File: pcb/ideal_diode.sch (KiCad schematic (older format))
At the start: 17 parts, among them P1 CONN_01X03, Q1 BSC028N06NS, Q2 BSC028N06NS, U1 LTC4359

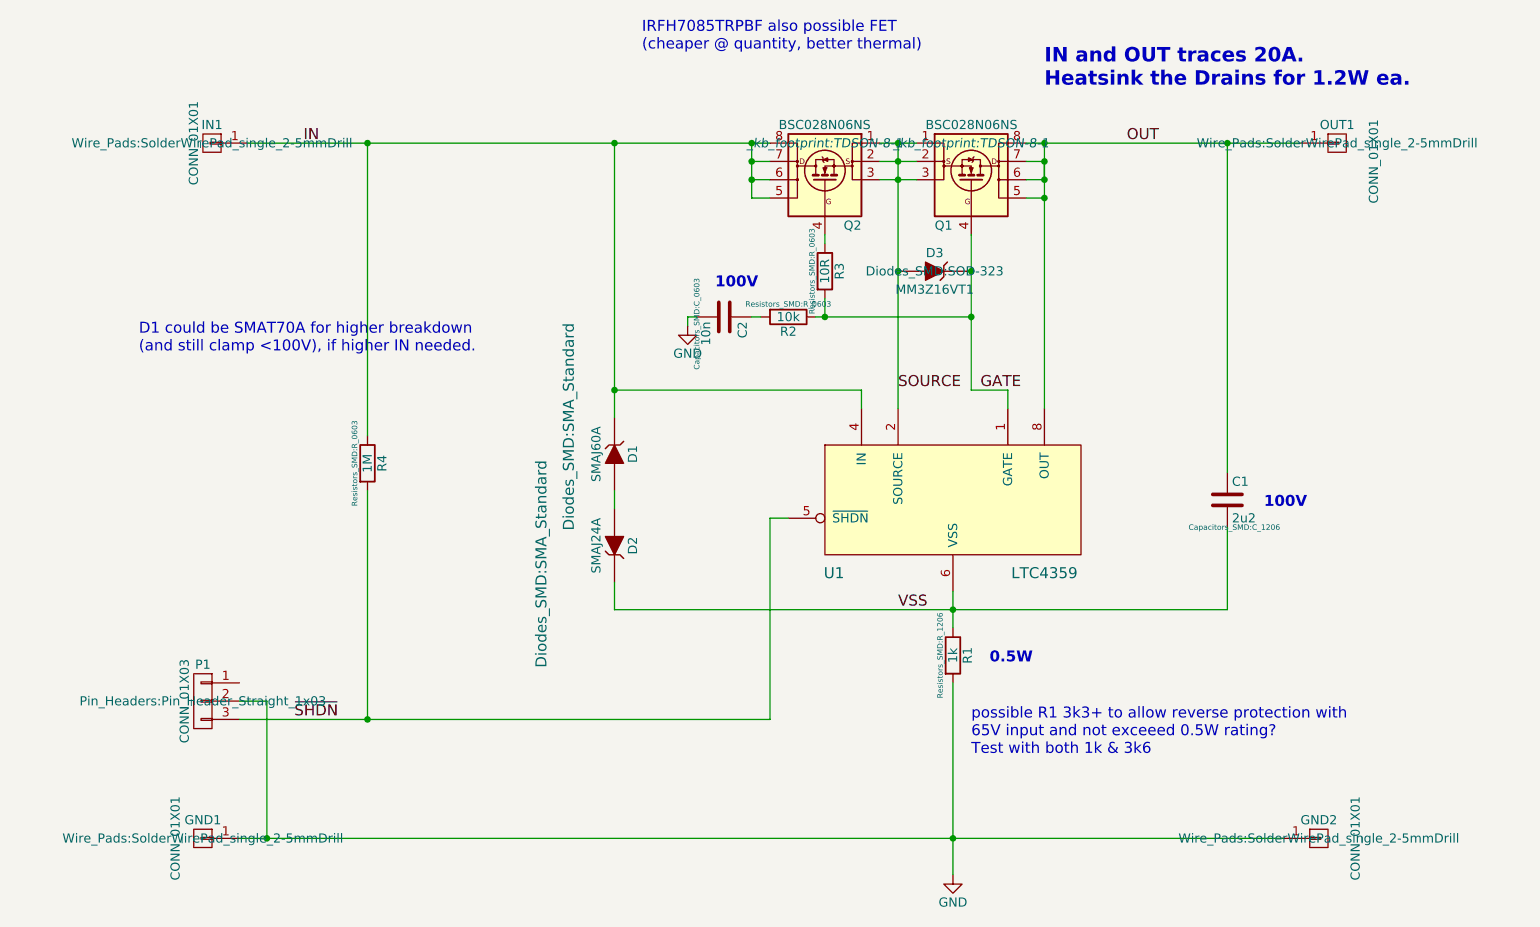
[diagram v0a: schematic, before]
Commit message: setting license as CERN OHL updating titleblocks ready for 1.0 release, added silkscreen ID & version. changed from 4V-70V to 5V-60V to reflect design capabilities changed R1 from 1k to 3k6 & removed text note added description, manufacturer, part number & supplier info for all RS parts added TODO text doc
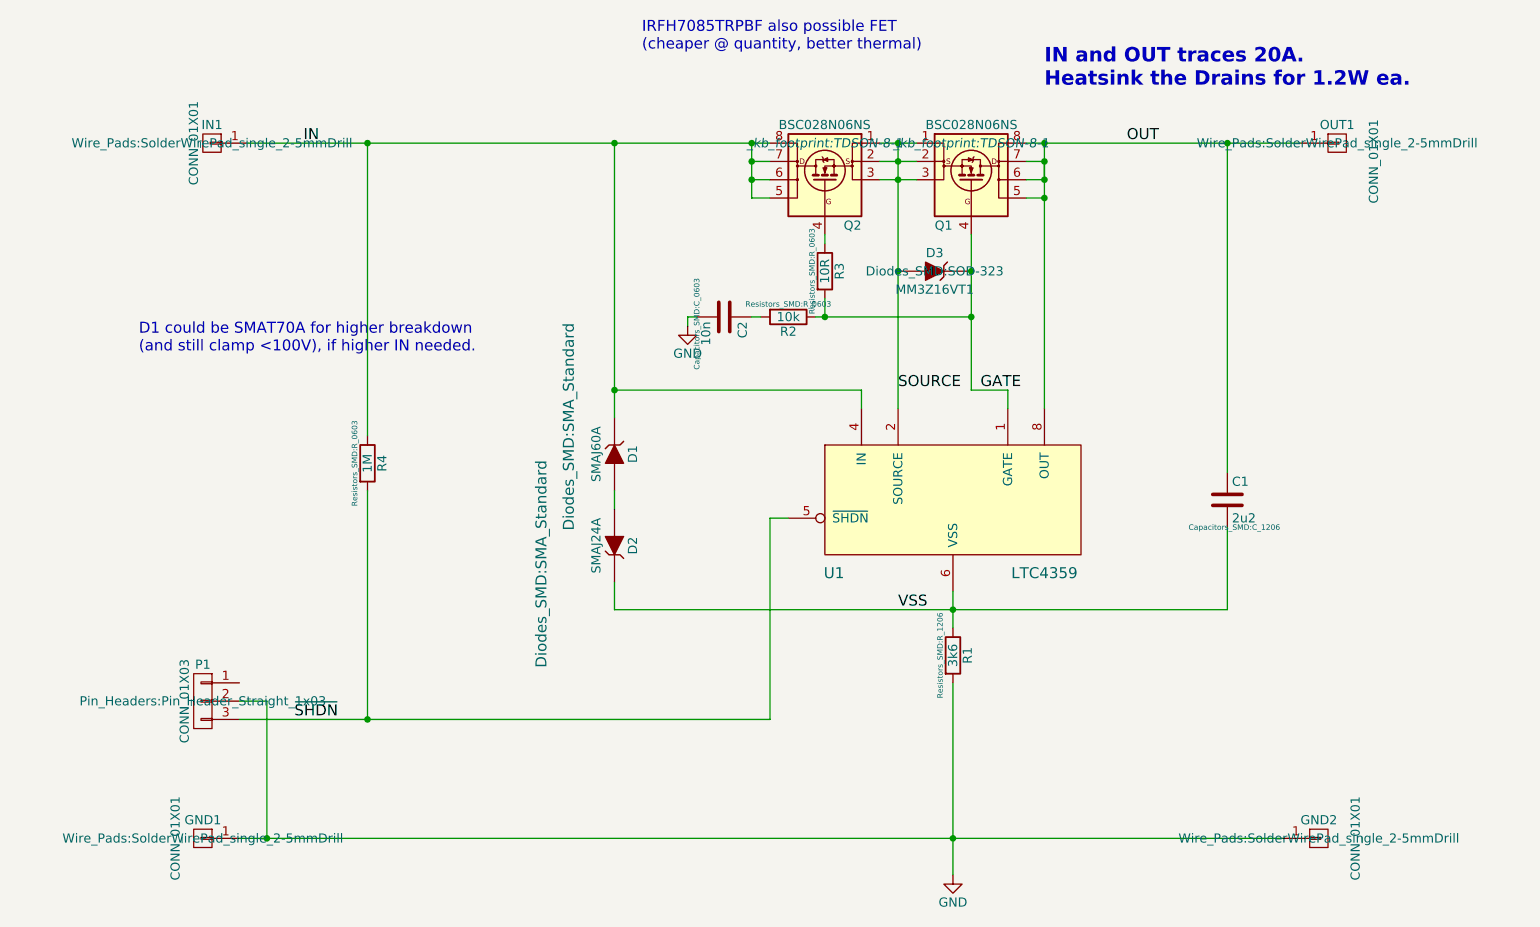
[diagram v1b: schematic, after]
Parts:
- C1: Description (none) -> 1206 100V X7R 10% Capacitor; Fit (none) -> True; ManufacturerName (none) -> Murata; ManufacturerPart (none) -> GRM31CR72A225KA73L; rs (none) -> 8202863
- C2: Description (none) -> 0603 100V X7R 10% Capacitor; Fit (none) -> True; ManufacturerName (none) -> AVX; ManufacturerPart (none) -> 06031C103K4Z2A; rs (none) -> 6983210
- D1: Description (none) -> 60V TVS 400W SMA; Fit (none) -> True; ManufacturerName (none) -> Taiwan Semi; ManufacturerPart (none) -> SMAJ60A; rs (none) -> 6873368
- D2: Description (none) -> 24V TVS 400W SMA; Fit (none) -> True; ManufacturerName (none) -> Taiwan Semi; ManufacturerPart (none) -> SMAJ24A; rs (none) -> 7485161
- D3: Description (none) -> 16V 6% 0.2W Zener Diode SOD-323; Fit (none) -> True; ManufacturerName (none) -> ON Semi; ManufacturerPart (none) -> MM3Z16VT1G; rs (none) -> 6878212
- GND1, GND2, IN1, OUT1: Description (none) -> _; Fit (none) -> False; ManufacturerName (none) -> _; ManufacturerPart (none) -> _; rs (none) -> _
- P1: Description (none) -> 1x3way 2.54mm Header; Fit (none) -> True; ManufacturerName (none) -> _; ManufacturerPart (none) -> _; rs (none) -> _
- Q1, Q2: Description (none) -> N-Channel 60V 100A TDSON8; Fit (none) -> True; ManufacturerName (none) -> Infineon; ManufacturerPart (none) -> BSC028N06NS; rs (none) -> 9064296
- R1: value 1k -> 3k6; Description (none) -> 0.5W 1206 Resistor; Fit (none) -> True; ManufacturerName (none) -> Panasonic; ManufacturerPart (none) -> ERJP08F3601V; rs (none) -> 7219866
- R2, R3, R4: Description (none) -> 0603 Resistor; Fit (none) -> True; ManufacturerName (none) -> _; ManufacturerPart (none) -> _; rs (none) -> _
- U1: Description (none) -> Ideal Diode Controller MSOP-8; Fit (none) -> True; ManufacturerName (none) -> Linear Tech; ManufacturerPart (none) -> LTC4359IMS8; rs (none) -> 8516843
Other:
- note removed: "0.5W"
- note removed: "100V"
- note removed: "possible R1 3k3+ to allow reverse protection with\n65V input and not exceeed 0.5W rating?\nTest with both 1k & 3k6"
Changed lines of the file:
@@
 encoding utf-8
 Sheet 1 1
-Title "20A Ideal Diode LTC4359 4V-70V"
-Date "2016-01-22"
-Rev "0.9"
+Title "20A Ideal Diode LTC4359 5V-60V"
+Date "2016-12-10"
+Rev "1.0"
 Comp ""
 Comment1 ""
@@
 F 2 "Housings_SSOP:MSOP-8_3x3mm_Pitch0.65mm" H 6000 3550 60  0001 C CNN
 F 3 "" H 6000 3550 60  0000 C CNN
+F 4 "Linear Tech" H 6000 3550 60  0001 C CNN "ManufacturerName"
+F 5 "LTC4359IMS8" H 6000 3550 60  0001 C CNN "ManufacturerPart"
+F 6 "Ideal Diode Controller MSOP-8" H 6000 3550 60  0001 C CNN "Description"
+F 7 "True" H 6000 3550 60  0001 C CNN "Fit"
+F 8 "8516843" H 6000 3550 60  0001 C CNN "rs"
 	1    6000 3550
 	1    0    0    -1
@@
 F 2 "Capacitors_SMD:C_1206" H 7538 3400 30  0000 C CNN
 F 3 "" H 7500 3550 60  0000 C CNN
+F 4 "Murata" H 7500 3550 60  0001 C CNN "ManufacturerName"
+F 5 "GRM31CR72A225KA73L" H 7500 3550 60  0001 C CNN "ManufacturerPart"
+F 6 "1206 100V X7R 10% Capacitor" H 7500 3550 60  0001 C CNN "Description"
+F 7 "True" H 7500 3550 60  0001 C CNN "Fit"
+F 8 "8202863" H 7500 3550 60  0001 C CNN "rs"
 	1    7500 3550
 	1    0    0    -1
@@
 P 6000 4400
 F 0 "R1" V 6080 4400 50  0000 C CNN
-F 1 "1k" V 6000 4400 50  0000 C CNN
+F 1 "3k6" V 6000 4400 50  0000 C CNN
 F 2 "Resistors_SMD:R_1206" V 5930 4400 30  0000 C CNN
 F 3 "" H 6000 4400 30  0000 C CNN
+F 4 "Panasonic" H 6000 4400 60  0001 C CNN "ManufacturerName"
+F 5 "ERJP08F3601V" H 6000 4400 60  0001 C CNN "ManufacturerPart"
+F 6 "0.5W 1206 Resistor" H 6000 4400 60  0001 C CNN "Description"
+F 7 "True" H 6000 4400 60  0001 C CNN "Fit"
+F 8 "7219866" H 6000 4400 60  0001 C CNN "rs"
 	1    6000 4400
 	1    0    0    -1
@@
 F 2 "_kb_footprint:TDSON-8-1" H 6100 2000 50  0000 C CIN
 F 3 "" V 6100 1800 50  0000 L CNN
+F 4 "Infineon" H 6100 1800 60  0001 C CNN "ManufacturerName"
+F 5 "BSC028N06NS" H 6100 1800 60  0001 C CNN "ManufacturerPart"
+F 6 "N-Channel 60V 100A TDSON8" H 6100 1800 60  0001 C CNN "Description"
+F 7 "True" H 6100 1800 60  0001 C CNN "Fit"
+F 8 "9064296" H 6100 1800 60  0001 C CNN "rs"
 	1    6100 1800
 	1    0    0    -1
@@
 F 2 "Diodes_SMD:SMA_Standard" H 4000 3050 60  0000 C CNN
 F 3 "" H 4150 3300 60  0000 C CNN
+F 4 "Taiwan Semi" H 4150 3300 60  0001 C CNN "ManufacturerName"
+F 5 "SMAJ60A" H 4150 3300 60  0001 C CNN "ManufacturerPart"
+F 6 "60V TVS 400W SMA" H 4150 3300 60  0001 C CNN "Description"
+F 7 "True" H 4150 3300 60  0001 C CNN "Fit"
+F 8 "6873368" H 4150 3300 60  0001 C CNN "rs"
 	1    4150 3300
 	0    1    1    0
@@
 F 2 "Diodes_SMD:SMA_Standard" H 4050 3400 60  0000 C CNN
 F 3 "" H 4150 3800 60  0000 C CNN
+F 4 "Taiwan Semi" H 4150 3800 60  0001 C CNN "ManufacturerName"
+F 5 "SMAJ24A" H 4150 3800 60  0001 C CNN "ManufacturerPart"
+F 6 "24V TVS 400W SMA" H 4150 3800 60  0001 C CNN "Description"
+F 7 "True" H 4150 3800 60  0001 C CNN "Fit"
+F 8 "7485161" H 4150 3800 60  0001 C CNN "rs"
 	1    4150 3800
 	0    1    -1   0
@@
 F 2 "_kb_footprint:TDSON-8-1" H 5300 2000 50  0000 C CIN
 F 3 "" V 5300 1800 50  0000 L CNN
+F 4 "Infineon" H 5300 1800 60  0001 C CNN "ManufacturerName"
+F 5 "BSC028N06NS" H 5300 1800 60  0001 C CNN "ManufacturerPart"
+F 6 "N-Channel 60V 100A TDSON8" H 5300 1800 60  0001 C CNN "Description"
+F 7 "True" H 5300 1800 60  0001 C CNN "Fit"
+F 8 "9064296" H 5300 1800 60  0001 C CNN "rs"
 	1    5300 1800
 	-1   0    0    -1
@@
 F 2 "Diodes_SMD:SOD-323" H 5900 2300 50  0000 C CNN
 F 3 "" H 5900 2300 50  0000 C CNN
+F 4 "ON Semi" H 5900 2300 60  0001 C CNN "ManufacturerName"
+F 5 "MM3Z16VT1G" H 5900 2300 60  0001 C CNN "ManufacturerPart"
+F 6 "16V 6% 0.2W Zener Diode SOD-323" H 5900 2300 60  0001 C CNN "Description"
+F 7 "True" H 5900 2300 60  0001 C CNN "Fit"
+F 8 "6878212" H 5900 2300 60  0001 C CNN "rs"
 	1    5900 2300
 	-1   0    0    -1
@@
 F 2 "Resistors_SMD:R_0603" V 5230 2300 30  0000 C CNN
 F 3 "" H 5300 2300 30  0000 C CNN
+F 4 "_" H 5300 2300 60  0001 C CNN "ManufacturerName"
+F 5 "_" H 5300 2300 60  0001 C CNN "ManufacturerPart"
+F 6 "0603 Resistor" H 5300 2300 60  0001 C CNN "Description"
+F 7 "True" H 5300 2300 60  0001 C CNN "Fit"
+F 8 "_" H 5300 2300 60  0001 C CNN "rs"
 	1    5300 2300
 	1    0    0    -1
@@
 F 2 "Resistors_SMD:R_0603" V 5030 2550 30  0000 C CNN
 F 3 "" H 5100 2550 30  0000 C CNN
+F 4 "_" H 5100 2550 60  0001 C CNN "ManufacturerName"
+F 5 "_" H 5100 2550 60  0001 C CNN "ManufacturerPart"
+F 6 "0603 Resistor" H 5100 2550 60  0001 C CNN "Description"
+F 7 "True" H 5100 2550 60  0001 C CNN "Fit"
+F 8 "_" H 5100 2550 60  0001 C CNN "rs"
 	1    5100 2550
 	0    1    1    0
@@
 F 2 "Capacitors_SMD:C_0603" H 4788 2400 30  0000 C CNN
 F 3 "" H 4750 2550 60  0000 C CNN
+F 4 "AVX" H 4750 2550 60  0001 C CNN "ManufacturerName"
+F 5 "06031C103K4Z2A" H 4750 2550 60  0001 C CNN "ManufacturerPart"
+F 6 "0603 100V X7R 10% Capacitor" H 4750 2550 60  0001 C CNN "Description"
+F 7 "True" H 4750 2550 60  0001 C CNN "Fit"
+F 8 "6983210" H 4750 2550 60  0001 C CNN "rs"
 	1    4750 2550
 	0    1    1    0
@@
 F 2 "Resistors_SMD:R_0603" V 2730 3350 30  0000 C CNN
 F 3 "" H 2800 3350 30  0000 C CNN
+F 4 "_" H 2800 3350 60  0001 C CNN "ManufacturerName"
+F 5 "_" H 2800 3350 60  0001 C CNN "ManufacturerPart"
+F 6 "0603 Resistor" H 2800 3350 60  0001 C CNN "Description"
+F 7 "True" H 2800 3350 60  0001 C CNN "Fit"
+F 8 "_" H 2800 3350 60  0001 C CNN "rs"
 	1    2800 3350
 	1    0    0    -1
@@
 F 2 "Wire_Pads:SolderWirePad_single_2-5mmDrill" H 8100 1600 50  0000 C CNN
 F 3 "" H 8100 1600 50  0000 C CNN
+F 4 "_" H 8100 1600 60  0001 C CNN "ManufacturerName"
+F 5 "_" H 8100 1600 60  0001 C CNN "ManufacturerPart"
+F 6 "_" H 8100 1600 60  0001 C CNN "Description"
+F 7 "False" H 8100 1600 60  0001 C CNN "Fit"
+F 8 "_" H 8100 1600 60  0001 C CNN "rs"
 	1    8100 1600
 	1    0    0    -1
@@
 F 2 "Wire_Pads:SolderWirePad_single_2-5mmDrill" H 8000 5400 50  0000 C CNN
 F 3 "" H 8000 5400 50  0000 C CNN
+F 4 "_" H 8000 5400 60  0001 C CNN "ManufacturerName"
+F 5 "_" H 8000 5400 60  0001 C CNN "ManufacturerPart"
+F 6 "_" H 8000 5400 60  0001 C CNN "Description"
+F 7 "False" H 8000 5400 60  0001 C CNN "Fit"
+F 8 "_" H 8000 5400 60  0001 C CNN "rs"
 	1    8000 5400
 	1    0    0    -1
@@
 F 2 "Wire_Pads:SolderWirePad_single_2-5mmDrill" H 1950 1600 50  0000 C CNN
 F 3 "" H 1950 1600 50  0000 C CNN
+F 4 "_" H 1950 1600 60  0001 C CNN "ManufacturerName"
+F 5 "_" H 1950 1600 60  0001 C CNN "ManufacturerPart"
+F 6 "_" H 1950 1600 60  0001 C CNN "Description"
+F 7 "False" H 1950 1600 60  0001 C CNN "Fit"
+F 8 "_" H 1950 1600 60  0001 C CNN "rs"
 	1    1950 1600
 	-1   0    0    -1
@@
 F 2 "Wire_Pads:SolderWirePad_single_2-5mmDrill" H 1900 5400 50  0000 C CNN
 F 3 "" H 1900 5400 50  0000 C CNN
+F 4 "_" H 1900 5400 60  0001 C CNN "ManufacturerName"
+F 5 "_" H 1900 5400 60  0001 C CNN "ManufacturerPart"
+F 6 "_" H 1900 5400 60  0001 C CNN "Description"
+F 7 "False" H 1900 5400 60  0001 C CNN "Fit"
+F 8 "_" H 1900 5400 60  0001 C CNN "rs"
 	1    1900 5400
 	-1   0    0    -1
@@
 F 2 "Pin_Headers:Pin_Header_Straight_1x03" H 1900 4650 50  0000 C CNN
 F 3 "" H 1900 4650 50  0000 C CNN
+F 4 "_" H 1900 4650 60  0001 C CNN "ManufacturerName"
+F 5 "_" H 1900 4650 60  0001 C CNN "ManufacturerPart"
+F 6 "1x3way 2.54mm Header" H 1900 4650 60  0001 C CNN "Description"
+F 7 "True" H 1900 4650 60  0001 C CNN "Fit"
+F 8 "_" H 1900 4650 60  0001 C CNN "rs"
 	1    1900 4650
 	-1   0    0    -1
@@
 Text Notes 1550 2750 0    60   ~ 0
 D1 could be SMAT70A for higher breakdown\n(and still clamp <100V), if higher IN needed.
-Text Notes 6100 4950 0    60   ~ 0
-possible R1 3k3+ to allow reverse protection with\n65V input and not exceeed 0.5W rating?\nTest with both 1k & 3k6
-Text Notes 6200 4450 0    60   ~ 12
-0.5W
-Text Notes 4700 2400 0    60   ~ 12
-100V
-Text Notes 7700 3600 0    60   ~ 12
-100V
 $EndSCHEMATC

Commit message: last few changes for v1.0 Release Added part info for commodity R's and P1 Re-exported BOM and PCB data after minor changes since proto v0.9 added MPNs to one click BOM Updated readme & TODO, dates & version info etc moved drill files to /gerbers folder
Signed-off-by: Kevin Bibby <kevin@inanecoding.co.uk>
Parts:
- GND1, GND2, IN1, OUT1: Description _ -> Hole for solder / screw
- P1: ManufacturerName _ -> Harwin; ManufacturerPart _ -> M20-9990345; rs _ -> 6812975
- R2: ManufacturerName _ -> TE; ManufacturerPart _ -> CRG0603F10K; rs _ -> 2132418
- R3: ManufacturerName _ -> TE; ManufacturerPart _ -> CRG0603F10R; rs _ -> 2132008
- R4: ManufacturerName _ -> TE; ManufacturerPart _ -> CRG0603F1M0; rs _ -> 2132676
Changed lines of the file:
@@
 Sheet 1 1
 Title "20A Ideal Diode LTC4359 5V-60V"
-Date "2016-12-10"
+Date "2017-02-25"
 Rev "1.0"
 Comp ""
@@
 F 2 "Resistors_SMD:R_0603" V 5230 2300 30  0000 C CNN
 F 3 "" H 5300 2300 30  0000 C CNN
-F 4 "_" H 5300 2300 60  0001 C CNN "ManufacturerName"
-F 5 "_" H 5300 2300 60  0001 C CNN "ManufacturerPart"
+F 4 "TE" H 5300 2300 60  0001 C CNN "ManufacturerName"
+F 5 "CRG0603F10R" H 5300 2300 60  0001 C CNN "ManufacturerPart"
 F 6 "0603 Resistor" H 5300 2300 60  0001 C CNN "Description"
 F 7 "True" H 5300 2300 60  0001 C CNN "Fit"
-F 8 "_" H 5300 2300 60  0001 C CNN "rs"
+F 8 "2132008" H 5300 2300 60  0001 C CNN "rs"
 	1    5300 2300
 	1    0    0    -1
@@
 F 2 "Resistors_SMD:R_0603" V 5030 2550 30  0000 C CNN
 F 3 "" H 5100 2550 30  0000 C CNN
-F 4 "_" H 5100 2550 60  0001 C CNN "ManufacturerName"
-F 5 "_" H 5100 2550 60  0001 C CNN "ManufacturerPart"
+F 4 "TE" H 5100 2550 60  0001 C CNN "ManufacturerName"
+F 5 "CRG0603F10K" H 5100 2550 60  0001 C CNN "ManufacturerPart"
 F 6 "0603 Resistor" H 5100 2550 60  0001 C CNN "Description"
 F 7 "True" H 5100 2550 60  0001 C CNN "Fit"
-F 8 "_" H 5100 2550 60  0001 C CNN "rs"
+F 8 "2132418" H 5100 2550 60  0001 C CNN "rs"
 	1    5100 2550
 	0    1    1    0
@@
 F 2 "Resistors_SMD:R_0603" V 2730 3350 30  0000 C CNN
 F 3 "" H 2800 3350 30  0000 C CNN
-F 4 "_" H 2800 3350 60  0001 C CNN "ManufacturerName"
-F 5 "_" H 2800 3350 60  0001 C CNN "ManufacturerPart"
+F 4 "TE" H 2800 3350 60  0001 C CNN "ManufacturerName"
+F 5 "CRG0603F1M0" H 2800 3350 60  0001 C CNN "ManufacturerPart"
 F 6 "0603 Resistor" H 2800 3350 60  0001 C CNN "Description"
 F 7 "True" H 2800 3350 60  0001 C CNN "Fit"
-F 8 "_" H 2800 3350 60  0001 C CNN "rs"
+F 8 "2132676" H 2800 3350 60  0001 C CNN "rs"
 	1    2800 3350
 	1    0    0    -1
@@
 F 4 "_" H 8100 1600 60  0001 C CNN "ManufacturerName"
 F 5 "_" H 8100 1600 60  0001 C CNN "ManufacturerPart"
-F 6 "_" H 8100 1600 60  0001 C CNN "Description"
+F 6 "Hole for solder / screw" H 8100 1600 60  0001 C CNN "Description"
 F 7 "False" H 8100 1600 60  0001 C CNN "Fit"
 F 8 "_" H 8100 1600 60  0001 C CNN "rs"
@@
 F 4 "_" H 8000 5400 60  0001 C CNN "ManufacturerName"
 F 5 "_" H 8000 5400 60  0001 C CNN "ManufacturerPart"
-F 6 "_" H 8000 5400 60  0001 C CNN "Description"
+F 6 "Hole for solder / screw" H 8000 5400 60  0001 C CNN "Description"
 F 7 "False" H 8000 5400 60  0001 C CNN "Fit"
 F 8 "_" H 8000 5400 60  0001 C CNN "rs"
@@
 F 4 "_" H 1950 1600 60  0001 C CNN "ManufacturerName"
 F 5 "_" H 1950 1600 60  0001 C CNN "ManufacturerPart"
-F 6 "_" H 1950 1600 60  0001 C CNN "Description"
+F 6 "Hole for solder / screw" H 1950 1600 60  0001 C CNN "Description"
 F 7 "False" H 1950 1600 60  0001 C CNN "Fit"
 F 8 "_" H 1950 1600 60  0001 C CNN "rs"
@@
 F 4 "_" H 1900 5400 60  0001 C CNN "ManufacturerName"
 F 5 "_" H 1900 5400 60  0001 C CNN "ManufacturerPart"
-F 6 "_" H 1900 5400 60  0001 C CNN "Description"
+F 6 "Hole for solder / screw" H 1900 5400 60  0001 C CNN "Description"
 F 7 "False" H 1900 5400 60  0001 C CNN "Fit"
 F 8 "_" H 1900 5400 60  0001 C CNN "rs"
@@
 F 2 "Pin_Headers:Pin_Header_Straight_1x03" H 1900 4650 50  0000 C CNN
 F 3 "" H 1900 4650 50  0000 C CNN
-F 4 "_" H 1900 4650 60  0001 C CNN "ManufacturerName"
-F 5 "_" H 1900 4650 60  0001 C CNN "ManufacturerPart"
+F 4 "Harwin" H 1900 4650 60  0001 C CNN "ManufacturerName"
+F 5 "M20-9990345" H 1900 4650 60  0001 C CNN "ManufacturerPart"
 F 6 "1x3way 2.54mm Header" H 1900 4650 60  0001 C CNN "Description"
 F 7 "True" H 1900 4650 60  0001 C CNN "Fit"
-F 8 "_" H 1900 4650 60  0001 C CNN "rs"
+F 8 "6812975" H 1900 4650 60  0001 C CNN "rs"
 	1    1900 4650
 	-1   0    0    -1
